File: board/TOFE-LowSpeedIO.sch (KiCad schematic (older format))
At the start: 40 parts, among them P1 CONN_6X2, P2 CONN_6X2, P3 CONN_6X2, P4 CONN_6X2, P5 CONN_2, P6 CONN_6, SW1 SW_PUSH, SW2 SW_PUSH, SW3 SW_PUSH, SW4 SW_PUSH, U1 TOFE-8X, U2 AURD_COMM_SHIELD_ZERO_NEW, U3 PIC18F14K50, U5 7805_NW, X1 CRYSTAL, X2 USBMICRO

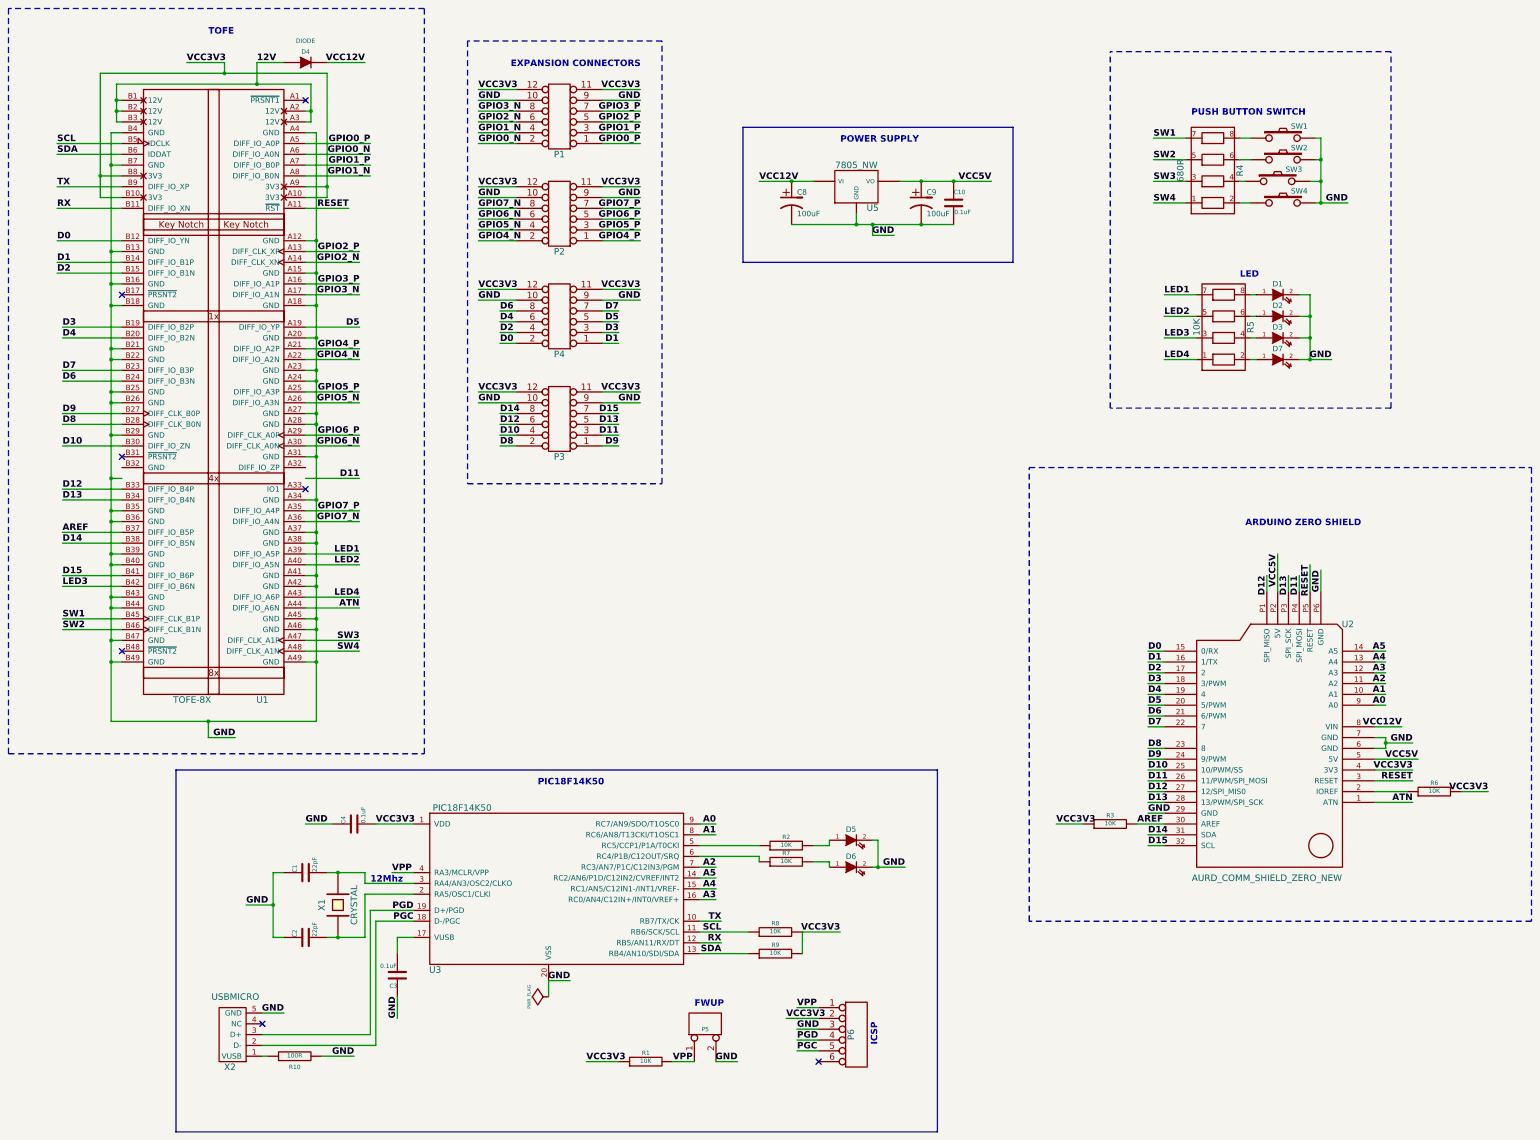
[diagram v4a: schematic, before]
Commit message: Fixing for TOFE part update.
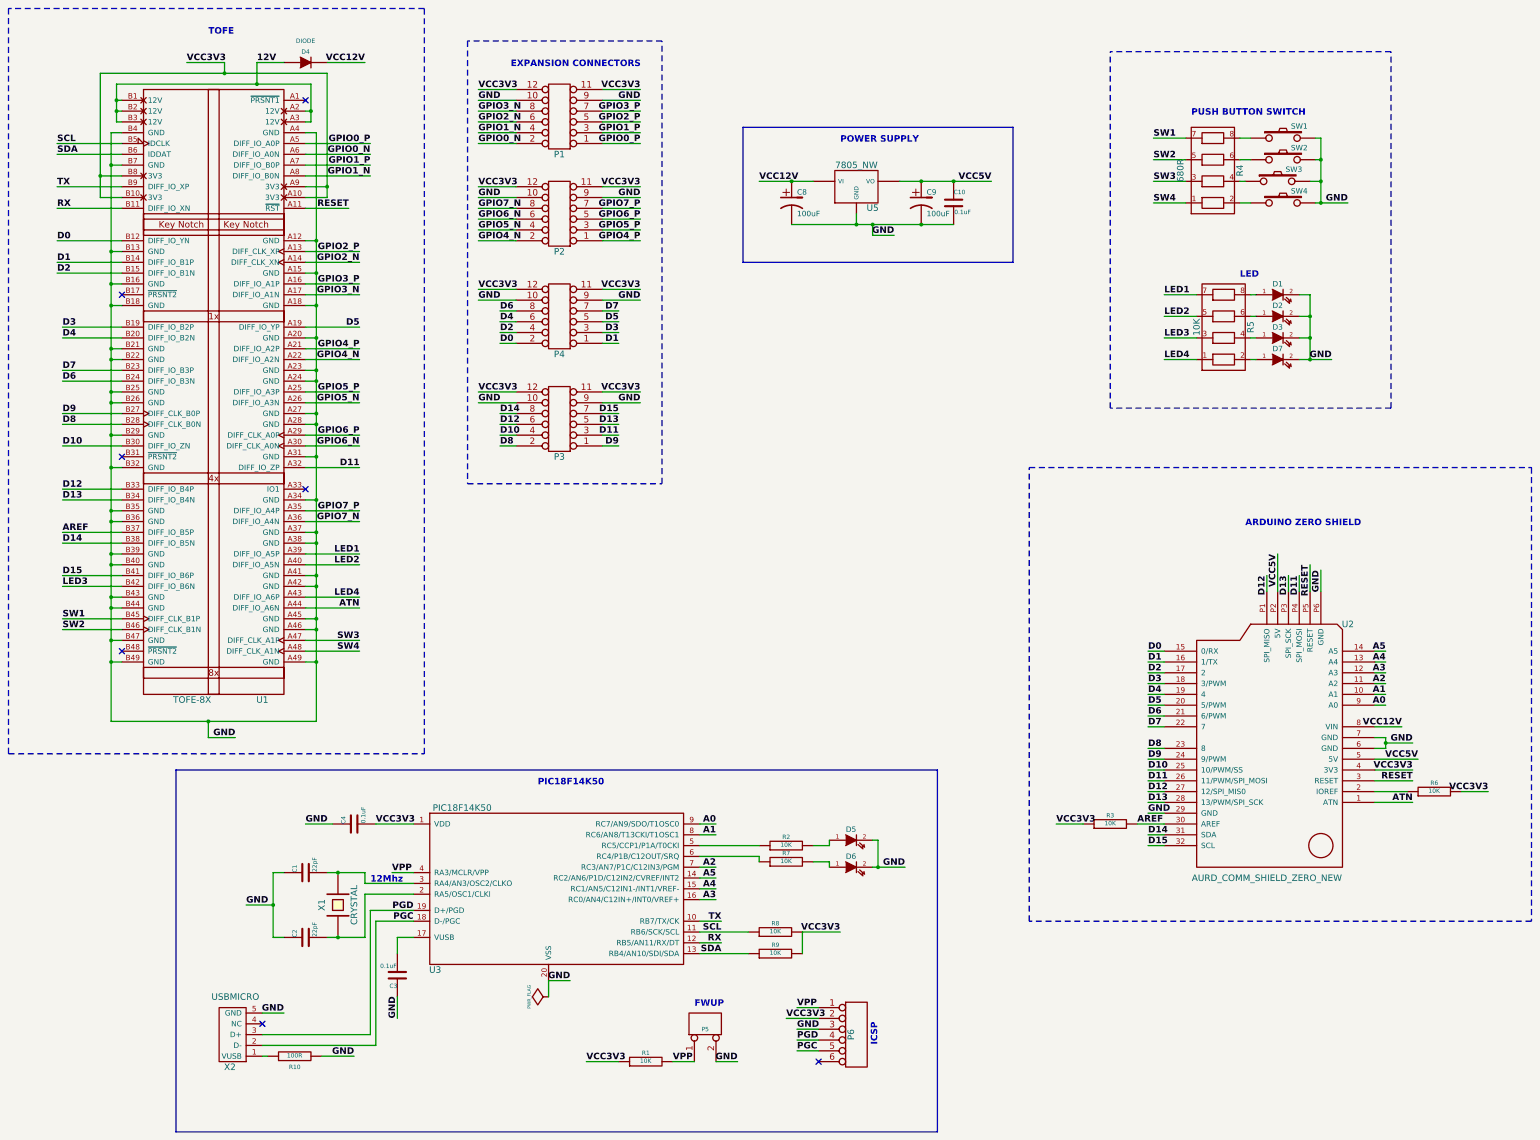
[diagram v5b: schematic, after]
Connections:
- net D11: now also U1.A32 (DIFF_IO_ZP)
- net GND: now also U1.B32 (GND)
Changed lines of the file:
@@
 Sheet 1 1
 Title "TOFE Low Speed IO Module"
-Date "2 nov 2015"
+Date "4 nov 2015"
 Rev ""
 Comp "Numato Lab"
@@
 Text Label 1750 4600 0    60   ~ 12
 D10
-Text Label 4500 4900 2    60   ~ 12
+Text Label 4500 4800 2    60   ~ 12
 D11
 Text Label 1750 5000 0    60   ~ 12
@@
 	2300 1700 2200 1700
 Wire Wire Line
-	2200 1700 2200 7150
+	2200 1700 2200 2000
+Wire Wire Line
+	2200 2000 2200 2800
+Wire Wire Line
+	2200 2800 2200 3100
+Wire Wire Line
+	2200 3100 2200 3300
+Wire Wire Line
+	2200 3300 2200 3700
+Wire Wire Line
+	2200 3700 2200 3800
+Wire Wire Line
+	2200 3800 2200 4100
+Wire Wire Line
+	2200 4100 2200 4200
+Wire Wire Line
+	2200 4200 2200 4500
+Wire Wire Line
+	2200 4500 2200 4800
+Wire Wire Line
+	2200 4800 2200 5200
+Wire Wire Line
+	2200 5200 2200 5300
+Wire Wire Line
+	2200 5300 2200 5600
+Wire Wire Line
+	2200 5600 2200 5700
+Wire Wire Line
+	2200 5700 2200 6000
+Wire Wire Line
+	2200 6000 2200 6100
+Wire Wire Line
+	2200 6100 2200 6400
+Wire Wire Line
+	2200 6400 2200 6600
+Wire Wire Line
+	2200 6600 2200 7150
 Wire Wire Line
 	2200 2000 2300 2000
@@
 Connection ~ 2200 4200
 Wire Wire Line
-	2200 4900 2300 4900
+	2200 4800 2300 4800
 Connection ~ 2200 4500
 Wire Wire Line
 	2200 5200 2300 5200
-Connection ~ 2200 4900
+Connection ~ 2200 4800
 Wire Wire Line
 	2200 5300 2300 5300
@@
 	4000 1700 4100 1700
 Wire Wire Line
-	4100 1700 4100 7150
+	4100 1700 4100 2700
+Wire Wire Line
+	4100 2700 4100 3000
+Wire Wire Line
+	4100 3000 4100 3300
+Wire Wire Line
+	4100 3300 4100 3600
+Wire Wire Line
+	4100 3600 4100 3900
+Wire Wire Line
+	4100 3900 4100 4000
+Wire Wire Line
+	4100 4000 4100 4300
+Wire Wire Line
+	4100 4300 4100 4400
+Wire Wire Line
+	4100 4400 4100 4700
+Wire Wire Line
+	4100 4700 4100 5100
+Wire Wire Line
+	4100 5100 4100 5400
+Wire Wire Line
+	4100 5400 4100 5500
+Wire Wire Line
+	4100 5500 4100 5800
+Wire Wire Line
+	4100 5800 4100 5900
+Wire Wire Line
+	4100 5900 4100 6200
+Wire Wire Line
+	4100 6200 4100 6300
+Wire Wire Line
+	4100 6300 4100 6600
+Wire Wire Line
+	4100 6600 4100 7150
 Wire Wire Line
 	4100 3000 4000 3000
@@
 Connection ~ 4100 6300
 Wire Wire Line
-	4100 7150 2200 7150
+	4100 7150 3100 7150
+Wire Wire Line
+	3100 7150 2200 7150
 Connection ~ 2200 6600
 Connection ~ 4100 6600
@@
 	4000 5200 4500 5200
 Wire Wire Line
-	4000 4900 4500 4900
+	4000 4800 4500 4800
 Wire Wire Line
 	4000 4600 4500 4600
@@
 	2100 2300 2300 2300
 Wire Wire Line
-	2100 1150 2100 2300
+	2100 1150 2100 2100
+Wire Wire Line
+	2100 2100 2100 2300
 Wire Wire Line
 	2100 2100 2300 2100
@@
 	4000 2200 4200 2200
 Wire Wire Line
-	4200 1150 4200 2300
+	4200 1150 4200 2200
+Wire Wire Line
+	4200 2200 4200 2300
 Wire Wire Line
 	4200 2300 4000 2300
 Wire Wire Line
-	2100 1150 4200 1150
+	2100 1150 3250 1150
+Wire Wire Line
+	3250 1150 4200 1150
 Connection ~ 4200 2200
 Connection ~ 2100 2100
@@
 	2250 1600 2300 1600
 Wire Wire Line
-	2250 1250 2250 1600
+	2250 1250 2250 1400
+Wire Wire Line
+	2250 1400 2250 1500
+Wire Wire Line
+	2250 1500 2250 1600
 Wire Wire Line
 	2250 1500 2300 1500
@@
 	4050 1600 4000 1600
 Wire Wire Line
-	4050 1250 4050 1600
+	4050 1250 4050 1500
+Wire Wire Line
+	4050 1500 4050 1600
 Wire Wire Line
 	4050 1500 4000 1500
 Wire Wire Line
-	2250 1250 4050 1250
+	2250 1250 3550 1250
+Wire Wire Line
+	3550 1250 4050 1250
 Connection ~ 4050 1500
 Connection ~ 2250 1400
@@
 	13900 7300 14000 7300
 Wire Wire Line
-	14000 7300 14000 7400
+	14000 7300 14000 7350
+Wire Wire Line
+	14000 7350 14000 7400
 Wire Wire Line
 	14000 7400 13900 7400
@@
 	11200 8100 10950 8100
 Wire Wire Line
-	8200 2150 8700 2150
-Wire Wire Line
-	8500 2550 10000 2550
+	8200 2150 8500 2150
+Wire Wire Line
+	8500 2150 8700 2150
+Wire Wire Line
+	8500 2550 9100 2550
+Wire Wire Line
+	9100 2550 9250 2550
+Wire Wire Line
+	9250 2550 9700 2550
+Wire Wire Line
+	9700 2550 10000 2550
 Wire Wire Line
 	9100 2550 9100 2450
@@
 	12250 3600 11950 3600
 Wire Wire Line
-	9500 2150 10350 2150
+	9500 2150 9700 2150
+Wire Wire Line
+	9700 2150 10000 2150
+Wire Wire Line
+	10000 2150 10350 2150
 Connection ~ 9700 2150
 Connection ~ 10000 2150
@@
 	3700 9150 3800 9150
 Wire Wire Line
-	3700 8550 3700 9150
+	3700 8550 3700 8850
+Wire Wire Line
+	3700 8850 3700 9150
 Wire Wire Line
 	3800 8550 3700 8550
 Connection ~ 4300 9150
 Wire Wire Line
-	4550 9150 4200 9150
+	4550 9150 4300 9150
+Wire Wire Line
+	4300 9150 4200 9150
 Wire Wire Line
 	4550 8750 4550 9150
@@
 Connection ~ 4300 8550
 Wire Wire Line
-	4550 8550 4200 8550
+	4550 8550 4300 8550
+Wire Wire Line
+	4300 8550 4200 8550
 Wire Wire Line
 	4550 8650 4550 8550
@@
 	9300 8250 9300 8500
 Wire Wire Line
-	9250 8500 9550 8500
+	9250 8500 9300 8500
+Wire Wire Line
+	9300 8500 9550 8500
 Connection ~ 9300 8500
 Wire Wire Line
@@
 	13200 3200 13300 3200
 Wire Wire Line
-	13300 3200 13300 3800
+	13300 3200 13300 3400
+Wire Wire Line
+	13300 3400 13300 3600
+Wire Wire Line
+	13300 3600 13300 3800
 Wire Wire Line
 	13300 3400 13200 3400
@@
 Connection ~ 13300 3400
 Wire Wire Line
-	13200 3800 13500 3800
+	13200 3800 13300 3800
+Wire Wire Line
+	13300 3800 13500 3800
 Connection ~ 13300 3600
 Connection ~ 13300 3800
@@
 	13350 1750 13400 1750
 Wire Wire Line
-	13400 1750 13400 2350
+	13400 1750 13400 1950
+Wire Wire Line
+	13400 1950 13400 2150
+Wire Wire Line
+	13400 2150 13400 2350
 Wire Wire Line
 	13400 1950 13350 1950
@@
 Connection ~ 13400 1950
 Wire Wire Line
-	13350 2350 13650 2350
+	13350 2350 13400 2350
+Wire Wire Line
+	13400 2350 13650 2350
 Connection ~ 13400 2150
 Connection ~ 13400 2350
